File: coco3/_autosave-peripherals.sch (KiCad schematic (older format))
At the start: 63 parts, among them CN2 Conn_01x16_Female, IC14 74LS30, IC15 74LS04, IC4 W65C21N6TPLG-14, IC5 W65C21N6TPLG-14, J1002 Conn_01x04_Male, Q1001 MMBT9014C, U1002 MAX3232, U1003 LM393, U3 LM393

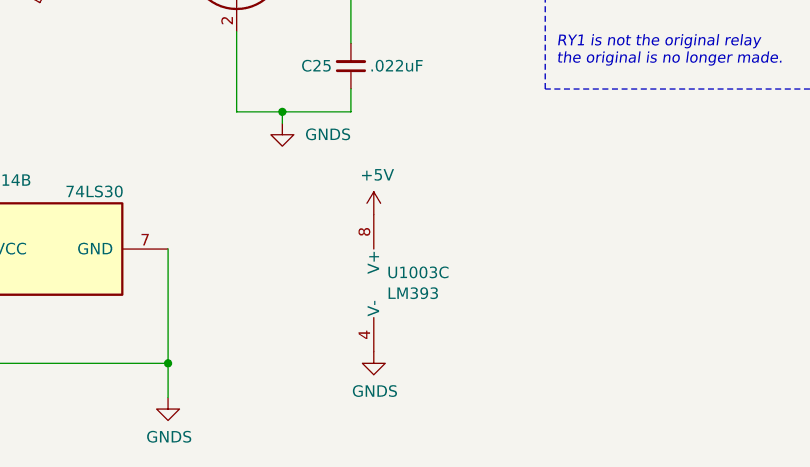
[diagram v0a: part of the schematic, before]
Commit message: added replacement circuitry for SC77526P DAC/ADC chip
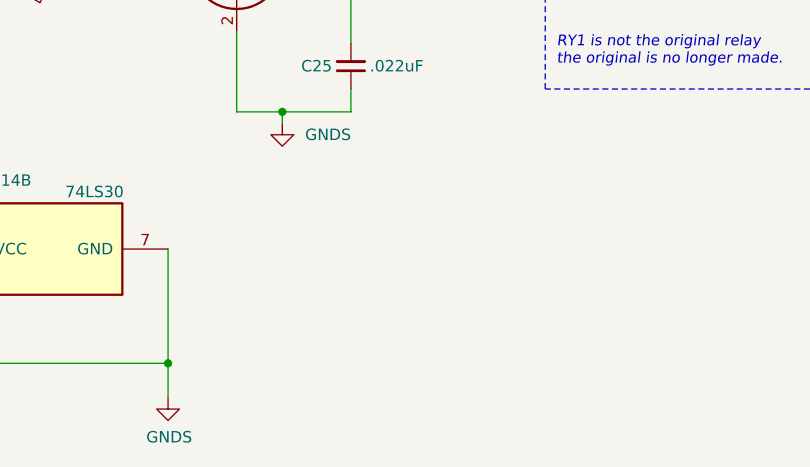
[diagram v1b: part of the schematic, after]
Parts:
- removed U1003: LM393, Package_SO:TSSOP-8_4.4x3mm_P0.65mm, symbol Comparator:LM393
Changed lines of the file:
@@
 Connection ~ 10550 1150
-$Comp
-L Comparator:LM393 U1003
-U 3 1 61E706EC
-P 8900 7300
-F 0 "U1003" H 8858 7346 50  0000 L CNN
-F 1 "LM393" H 8858 7255 50  0000 L CNN
-F 2 "Package_SO:TSSOP-8_4.4x3mm_P0.65mm" H 8900 7300 50  0001 C CNN
-F 3 "http://www.ti.com/lit/ds/symlink/lm393.pdf" H 8900 7300 50  0001 C CNN
-F 4 "LCSC" H 8900 7300 50  0001 C CNN "Vendor"
-F 5 "C160466" H 8900 7300 50  0001 C CNN "Vendor part#"
-F 6 "LM393PT" H 8900 7300 50  0001 C CNN "Manufacturer part#"
-	3    8900 7300
-	1    0    0    -1
-$EndComp
-$Comp
-L power:+5V #PWR?
-U 1 1 61E9C273
-P 8800 7000
-AR Path="/60273794/61E9C273" Ref="#PWR?"  Part="1"
-AR Path="/602A51A8/61E9C273" Ref="#PWR?"  Part="1"
-AR Path="/603CF7B8/61E9C273" Ref="#PWR01014"  Part="1"
-F 0 "#PWR01014" H 8800 6850 50  0001 C CNN
-F 1 "+5V" H 8815 7173 50  0000 C CNN
-F 2 "" H 8800 7000 50  0001 C CNN
-F 3 "" H 8800 7000 50  0001 C CNN
-	1    8800 7000
-	1    0    0    -1
-$EndComp
-$Comp
-L power:GNDS #PWR?
-U 1 1 61EA17D4
-P 8800 7600
-AR Path="/602A51A8/61EA17D4" Ref="#PWR?"  Part="1"
-AR Path="/603CF7B8/61EA17D4" Ref="#PWR01015"  Part="1"
-F 0 "#PWR01015" H 8800 7350 50  0001 C CNN
-F 1 "GNDS" H 8805 7427 50  0000 C CNN
-F 2 "" H 8800 7600 50  0001 C CNN
-F 3 "" H 8800 7600 50  0001 C CNN
-	1    8800 7600
-	1    0    0    -1
-$EndComp
 $Comp
 L Device:R_Small_US R?
